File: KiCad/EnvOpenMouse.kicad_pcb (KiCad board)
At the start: 2 copper layers, 34.5 x 42.7 mm, 48 parts, among them J1 SKRKAEE020, J2 SKRKAEE020, J3 Conn_01x03_Male, SW1 MouseSwitch, SW2 MouseSwitch, U1 TCR2EF19, U2 LM3671MF 3.3, U3 PMW3360DM-T2QU, U4 RP2040, Y1 Crystal 3225 12MHz

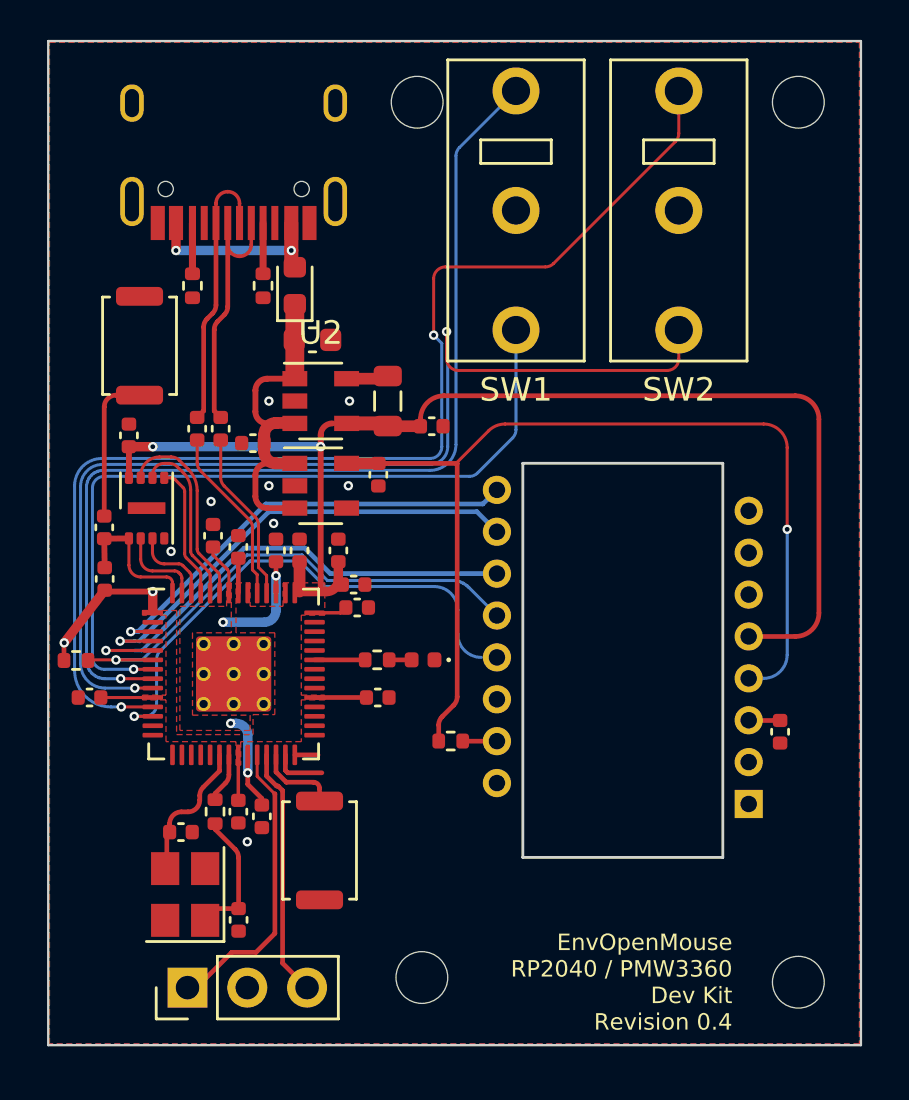
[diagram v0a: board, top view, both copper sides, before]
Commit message: added some GPIO headers
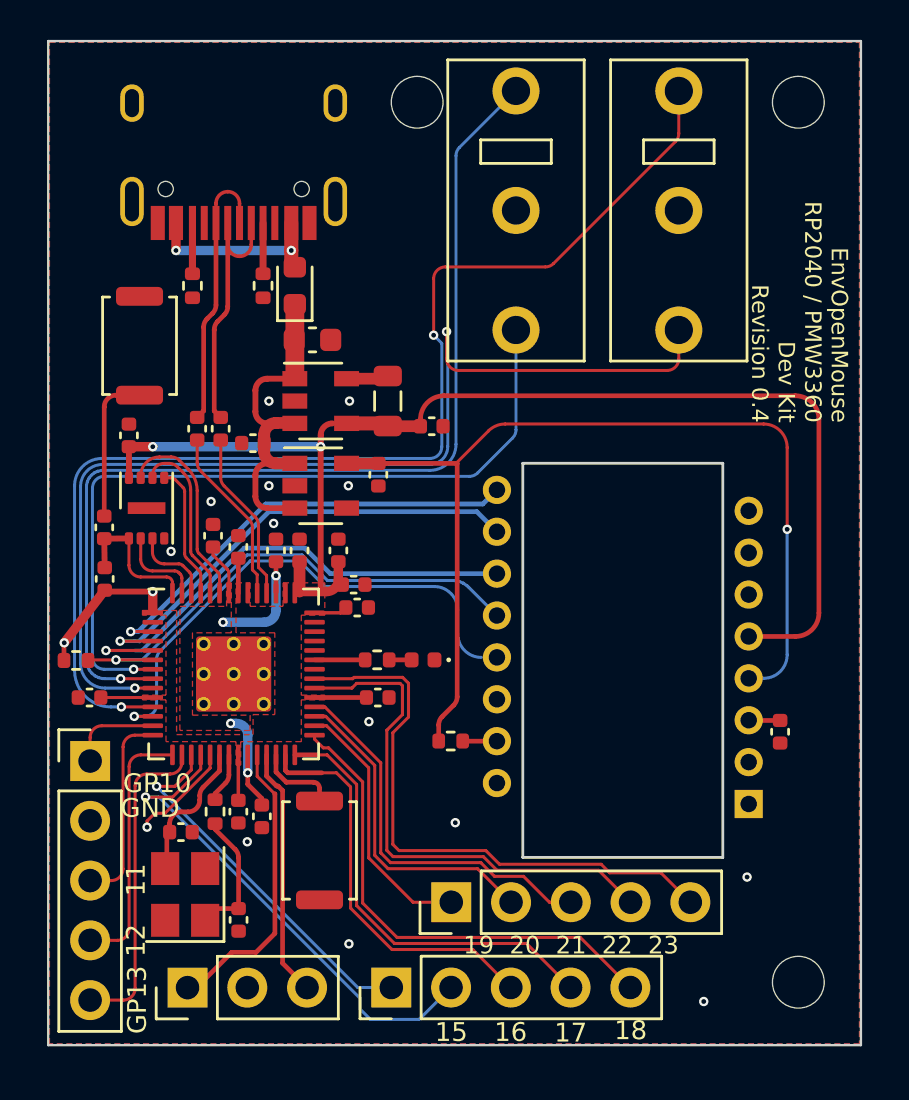
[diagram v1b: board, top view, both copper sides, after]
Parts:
- removed H3: MountingHole, MountingHole:MountingHole_2.2mm_M2
- added GPIOA1: Rotary_Encoder_Switch, Connector_PinHeader_2.54mm:PinHeader_1x05_P2.54mm_Vertical, F.Cu at (52.7, 70.2)
- added GPIOA2: Rotary_Encoder_Switch, Connector_PinHeader_2.54mm:PinHeader_1x05_P2.54mm_Vertical, F.Cu at (55.2, 66.6)
- added SCRL1: Rotary_Encoder_Switch, Connector_PinHeader_2.54mm:PinHeader_1x05_P2.54mm_Vertical, F.Cu at (39.9, 60.6)
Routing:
- net /GPIO23: track 0.00 -> 24.9 mm
- net /GPIO22: track 0.00 -> 22.4 mm
- net /GPIO15: track 0.00 -> 21.2 mm, vias 0 -> 1
- net /GPIO18: track 0.00 -> 21.0 mm
- net /GPIO17: track 0.99 -> 18.8 mm
- net /GPIO21: track 0.00 -> 16.6 mm
- net /GPIO14: track 0.00 -> 15.9 mm, vias 0 -> 1
- net /GPIO16: track 2.25 -> 17.1 mm
- net /GPIO20: track 0.00 -> 13.9 mm
- net /GPIO13: track 0.00 -> 13.6 mm
- net /GPIO19: track 0.00 -> 11.2 mm
- net /GPIO12: track 0.00 -> 10.9 mm
- net /GPIO11: track 0.00 -> 8.37 mm
- net GND: track 0.00 -> 4.43 mm, vias 8 -> 14
- net /GPIO10: track 0.00 -> 3.93 mm
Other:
- board text added: "11"
- board text added: "12"
- board text added: "15"
- board text added: "16"
- board text added: "17"
- board text added: "18"
- board text added: "19 20 21 22 23"
- board text added: "GND"
- board text added: "GP10"
- board text added: "GP13"

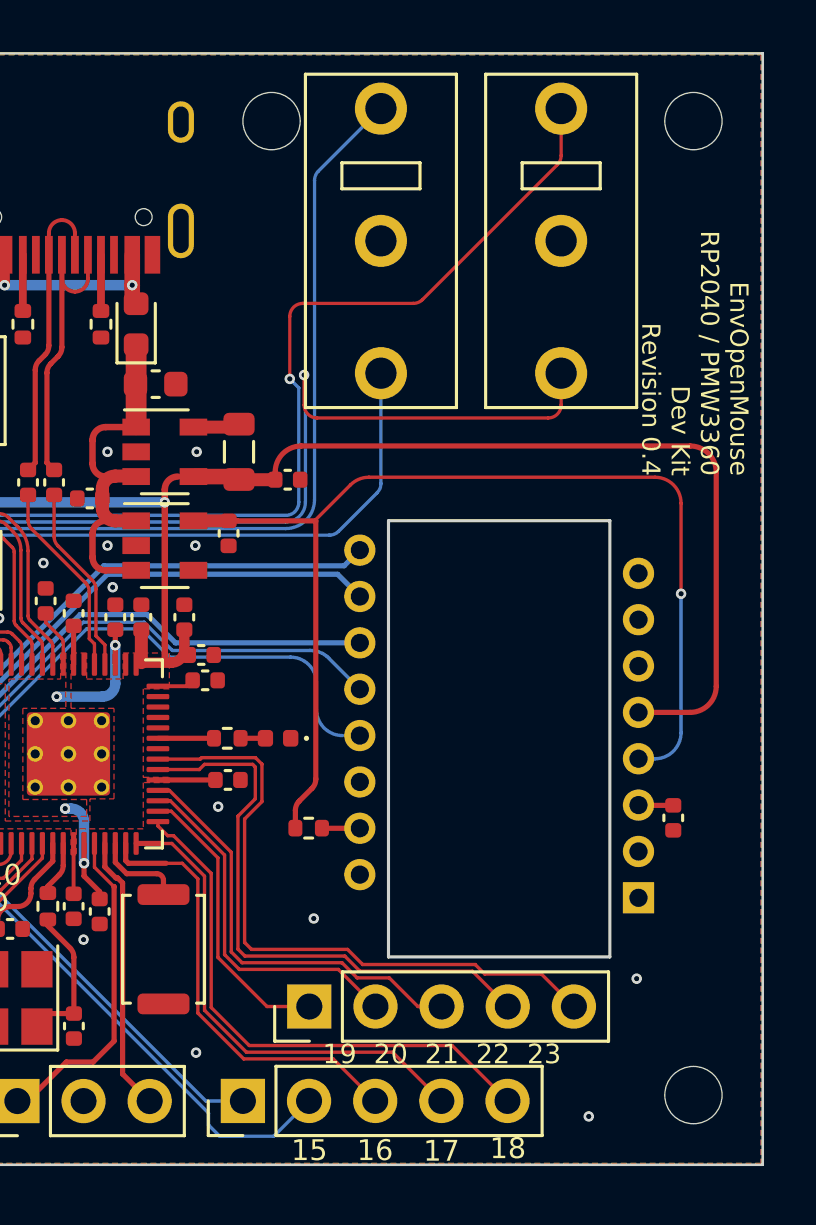
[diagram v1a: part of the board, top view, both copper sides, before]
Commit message: adjusted silkscreen markings and some traces.
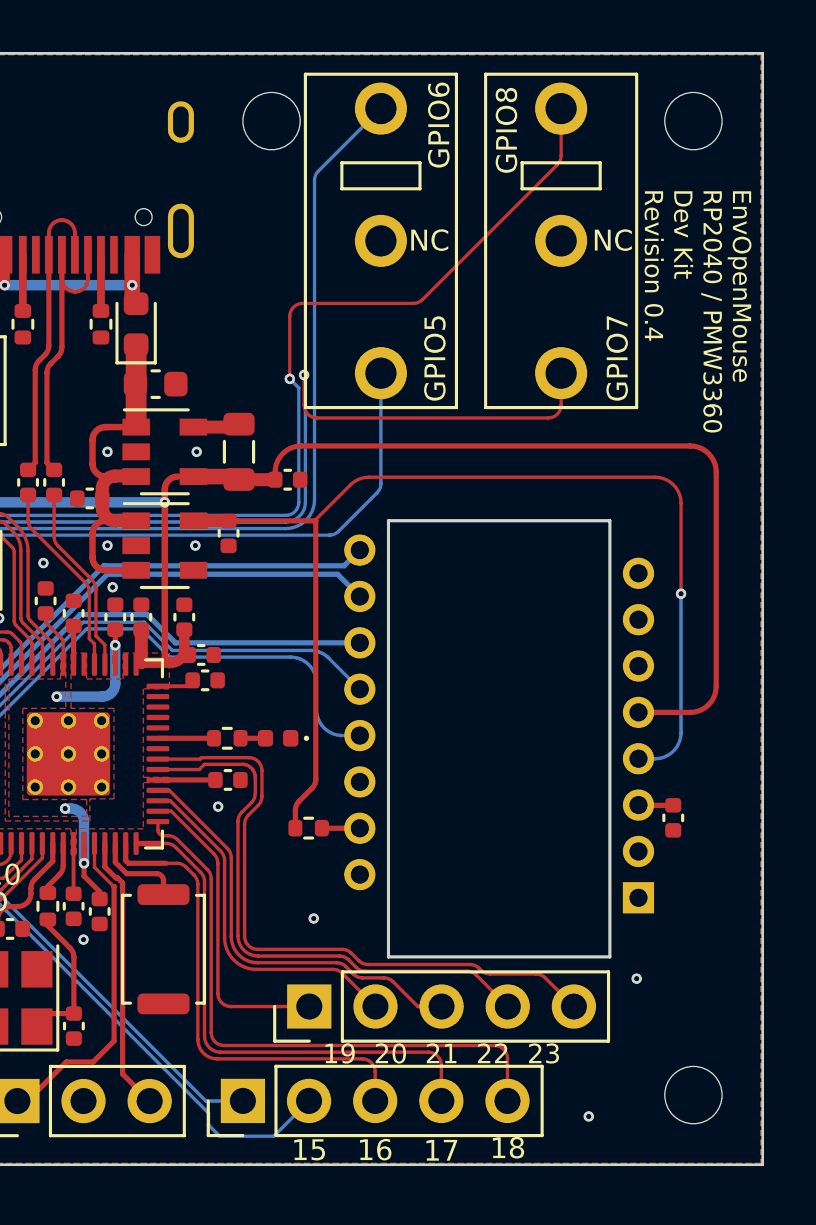
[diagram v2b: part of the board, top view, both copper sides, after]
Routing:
- net /GPIO18: track 21.0 -> 22.7 mm
- net /GPIO17: track 18.8 -> 20.3 mm
- net /GPIO16: track 17.1 -> 18.4 mm
- net /GPIO19: track 11.2 -> 12.0 mm
- net GND: vias 14 -> 13
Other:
- board text added: "GPIO5"
- board text added: "GPIO6"
- board text added: "GPIO7"
- board text added: "GPIO8"
- board text added: "NC"

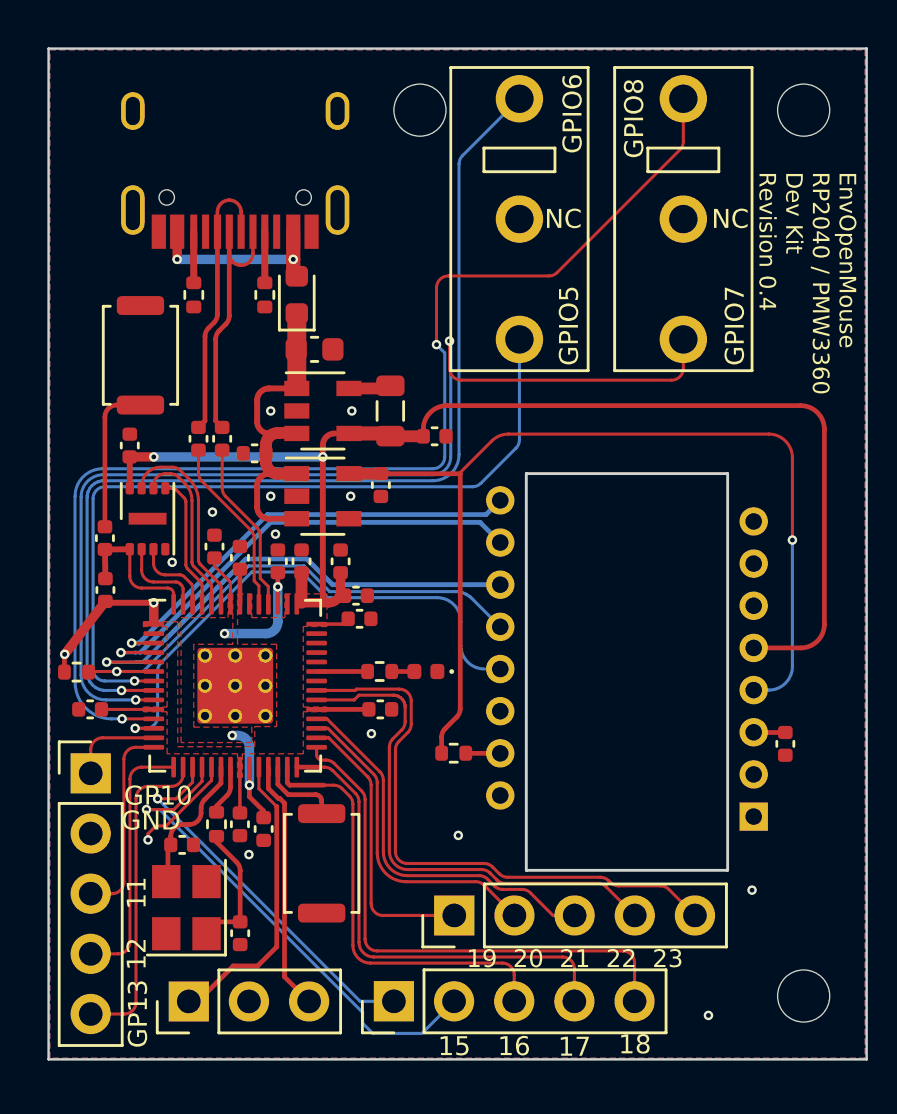
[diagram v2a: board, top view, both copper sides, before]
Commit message: swapped button bits for some GPIO headers
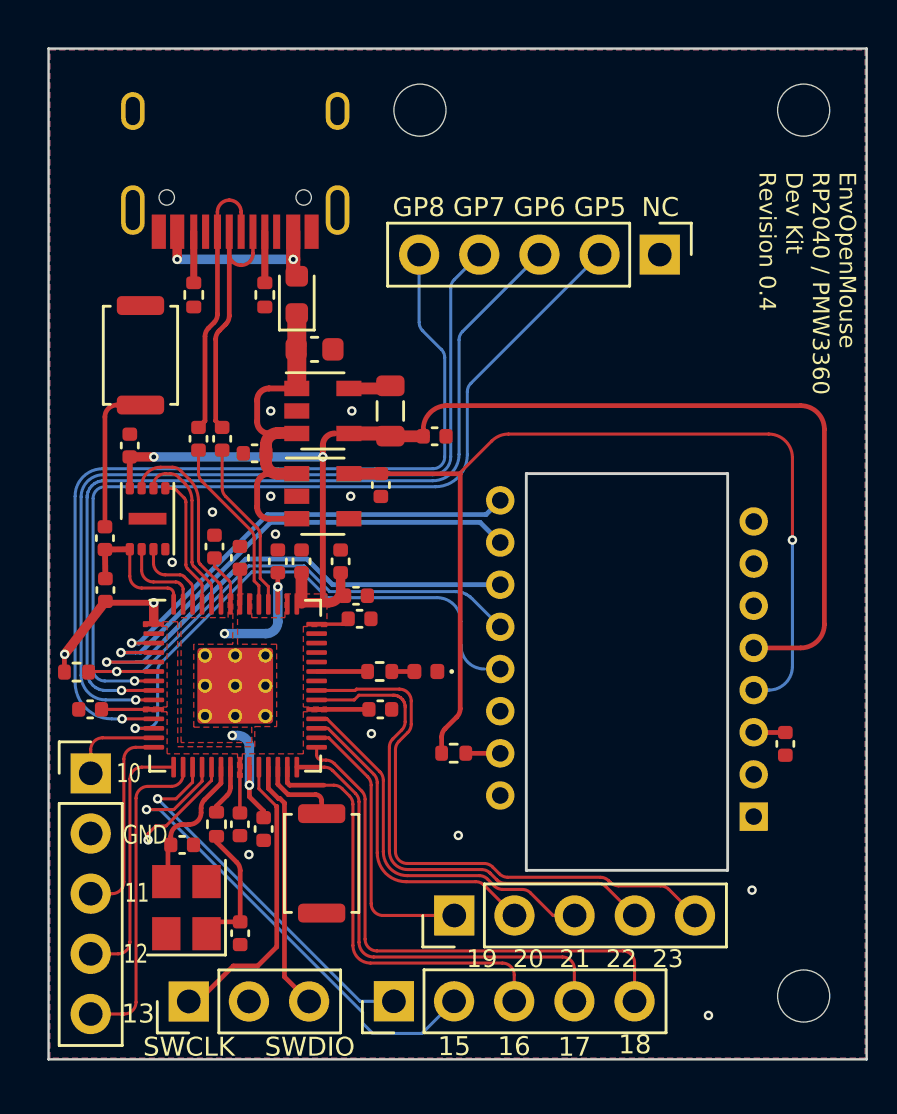
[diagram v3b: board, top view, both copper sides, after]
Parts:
- removed SW1, SW2: MouseSwitch, MouseSwitch:MouseSwitch
- added GPIOA3: GPIOs, Connector_PinHeader_2.54mm:PinHeader_1x05_P2.54mm_Vertical, F.Cu at (63.9, 38.7)
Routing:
- net /GPIO8: track 50.7 -> 37.4 mm, vias 2 -> 1
- net /GPIO7: track 45.4 -> 36.7 mm, vias 2 -> 1
- net /GPIO6: track 43.4 -> 37.1 mm
- net /GPIO5: track 33.5 -> 37.6 mm
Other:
- board text added: "10"
- board text added: "13"
- board text added: "GP5"
- board text added: "GP6"
- board text added: "GP7"
- board text added: "GP8"
- board text added: "SWCLK"
- board text added: "SWDIO"
- board text removed: "GP10"
- board text removed: "GP13"
- board text removed: "GPIO5"
- board text removed: "GPIO6"
- board text removed: "GPIO7"
- board text removed: "GPIO8"

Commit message: decided to overhaul this project a bit
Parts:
- removed C10, C11, C12, C13, C14, C17, C6, C7, C8, C9: 100nf 0402, Capacitor_SMD:C_0402_1005Metric
- removed C15, C16: 1uf 0402, Capacitor_SMD:C_0402_1005Metric
- removed C18, C19: 22pf 0402, Capacitor_SMD:C_0402_1005Metric
- removed C4: 10uf 0402, Capacitor_SMD:C_0402_1005Metric
- removed C5: 4.7uf 0402, Capacitor_SMD:C_0402_1005Metric
- removed D1: 1n4002 0603, Diode_SMD:D_0603_1608Metric
- removed D2: LED 0402 YELLOW, LED_SMD:LED_0402_1005Metric
- removed FLASH1: W25Q16FWUXIE, Package_SON:SON-8-1EP_3x2mm_P0.5mm_EP1.4x1.6mm
- removed GPIOA1, GPIOA2, SCRL1: Rotary_Encoder_Switch, Connector_PinHeader_2.54mm:PinHeader_1x05_P2.54mm_Vertical
- removed GPIOA3: GPIOs, Connector_PinHeader_2.54mm:PinHeader_1x05_P2.54mm_Vertical
- removed L1: INDUCTOR 2.2uH 0805, Inductor_SMD:L_0805_2012Metric
- removed R10: 1K 0402, Resistor_SMD:R_0402_1005Metric
- removed R3: 10K 0402, Resistor_SMD:R_0402_1005Metric
- removed R4: 5.1K, Resistor_SMD:R_0402_1005Metric
- removed R5: 10K 0402, Capacitor_SMD:C_0402_1005Metric
- removed R6, R7: 27Ohms 0402 Resistor, Capacitor_SMD:C_0402_1005Metric
- removed R8: 1k 0402 Resistor, Capacitor_SMD:C_0402_1005Metric
- removed R9: 470 ohm resistor, Resistor_SMD:R_0402_1005Metric
- removed U3: PMW3360DM-T2QU, local:DIP-16_W10.16mm
- removed U4: RP2040, env:RP2040-QFN-56
- removed Y1: Crystal 3225 12MHz, Crystal:Crystal_SMD_3225-4Pin_3.2x2.5mm
- removed e1: TYPE-C-31-M-12, Type-C:HRO-TYPE-C-31-M-12-Assembly
- added H10: MountingHole_Pad, MountingHole:MountingHole_2.2mm_M2, F.Cu at (57.5, 15.1)
- added H3: MountingHole_Pad, MountingHole:MountingHole_2.2mm_M2, F.Cu at (50.0, 15.0)
- added H5: MountingHole_Pad, MountingHole:MountingHole_2.2mm_M2, F.Cu at (33.5, 40.2)
- added H6: MountingHole_Pad, MountingHole:MountingHole_2.2mm_M2, F.Cu at (16.4, 14.9)
- added H7: MountingHole_Pad, MountingHole:MountingHole_2.2mm_M2, F.Cu at (33.5, 14.9)
- added H8: MountingHole_Pad, MountingHole:MountingHole_2.2mm_M2, F.Cu at (16.4, 40.2)
- added H9: MountingHole_Pad, MountingHole:MountingHole_2.2mm_M2, F.Cu at (60.1, 40.0)
- added J4: Conn_01x03, Connector_PinHeader_2.54mm:PinHeader_1x03_P2.54mm_Vertical, F.Cu at (62.6, 34.9)
- added SW1: SW_Push_SPDT, MouseSwitch:MouseSwitch, F.Cu at (40.7, 23.9)
- added SW2: SW_Push_SPDT, MouseSwitch:MouseSwitch, F.Cu at (50.0, 24.0)
- added VR1: EC10E1220501, EC10E1220501:TRIM_EC10E1220501, F.Cu at (60.8, 21.8)
- C1: value 10uf 0603 6.3V -> 0.1uf 0402; footprint Capacitor_SMD:C_0603_1608Metric -> Capacitor_SMD:C_0201_0603Metric
- C2: value 0.1uf 0402 -> 1uf 0402; footprint Capacitor_SMD:C_0402_1005Metric -> Capacitor_SMD:C_0201_0603Metric
- C3: value 1uf 0402 -> 4.7uf 0402; footprint Capacitor_SMD:C_0402_1005Metric -> Capacitor_SMD:C_0201_0603Metric
- H1, H2, H4: value MountingHole -> MountingHole_Pad
- J1: value SKRKAEE020 -> Conn_01x08; footprint Button_Switch_SMD:SW_Push_SPST_NO_Alps_SKRK -> Connector_PinHeader_1.00mm:PinHeader_1x08_P1.00mm_Vertical
- J2: value SKRKAEE020 -> Conn_01x03; footprint Button_Switch_SMD:SW_Push_SPST_NO_Alps_SKRK -> Connector_PinSocket_2.54mm:PinSocket_1x03_P2.54mm_Vertical
- J3: value Conn_01x03_Male -> Conn_01x03; footprint Connector_PinHeader_2.54mm:PinHeader_1x03_P2.54mm_Vertical -> Connector_PinSocket_2.54mm:PinSocket_1x03_P2.54mm_Vertical
- R2: value 5.1K -> 10K 0402
- U2: value LM3671MF 3.3 -> PMW3360DM-T2QU; footprint Package_TO_SOT_SMD:SOT-23-5 -> local:DIP-16_W10.16mm
- moved U1 43.2 mm to (17.6, 19.9)
- moved R1 41.7 mm to (33.9, 24.0), turned to 180 degrees
- moved C1 40.9 mm to (14.8, 20.9)
- moved C3 39.9 mm to (20.2, 24.6)
- moved C2 39.0 mm to (19.9, 18.9), turned to -90 degrees
- moved H4 38.7 mm to (50.0, 36.8)
- moved J3 38.0 mm to (47.5, 32.4)
- moved U2 37.2 mm to (22.6, 19.8)
- moved H1 34.2 mm to (40.7, 14.9)
- moved J2 34.0 mm to (38.1, 32.4), turned to 90 degrees
- moved J1 27.4 mm to (17.6, 30.5), turned to 180 degrees
- moved R2 17.4 mm to (33.9, 29.3), turned to 180 degrees
- moved H2 13.8 mm to (40.7, 36.8)
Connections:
- C1 pad 1: +5V -> GND
- C1 pad 2: GND -> +5V
- C2 pad 2: +5V -> +1V8
- C3 pad 1: GND -> Net-(C3-Pad1)
- C3 pad 2: +1V8 -> GND
- J1 pad 1: /~{USB_BOOT} -> NCS/GPIO9
- J1 pad 2: GND -> MISO/GPIO4
- J2 pad 1: /RUN -> Net-(J2-Pad1)
- J2 pad 2: GND -> Net-(J2-Pad2)
- J3 pad 1: /SWCLK -> Net-(J3-Pad1)
- J3 pad 2: GND -> Net-(J3-Pad2)
- J3 pad 3: /SWD -> Net-(J3-Pad3)
- R2 pad 1: GND -> +3V3
- R2 pad 2: Net-(R2-Pad2) -> MISO/GPIO4
- U2 pad 1: +5V -> unconnected-(U2-Pad1)
- U2 pad 2: GND -> unconnected-(U2-Pad2)
- U2 pad 3: +5V -> Net-(C3-Pad1)
- U2 pad 4: +3V3 -> +1V8
- U2 pad 5: Net-(L1-Pad1) -> +3V3
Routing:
- net /GPIO5: track 37.6 -> 0.00 mm, vias 1 -> 0
- net /GPIO8: track 37.4 -> 0.00 mm, vias 1 -> 0
- net /GPIO6: track 37.1 -> 0.00 mm, vias 1 -> 0
- net /GPIO7: track 36.7 -> 0.00 mm, vias 1 -> 0
- net NCS/GPIO9: track 0.00 -> 34.4 mm
- net MISO/GPIO4: track 0.00 -> 31.6 mm
- net +3V3: track 69.6 -> 38.0 mm, vias 4 -> 1
- net MOSI/GPIO3: track 0.00 -> 28.9 mm
- net SCLK/GPIO2: track 0.00 -> 26.7 mm
- net /GPIO23: track 24.6 -> 0.00 mm
- net MOTION/GPIO1: track 0.00 -> 23.8 mm
- net /GPIO18: track 22.7 -> 0.00 mm
- net NCS: track 22.1 -> 0.00 mm, vias 1 -> 0
- net /GPIO22: track 21.9 -> 0.00 mm
- net MISO: track 21.8 -> 0.00 mm, vias 1 -> 0
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- removed copper zone on F.Cu, net +1V1
- removed copper zone on F.Cu, net +3V3
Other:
- board size 34.5 x 42.7 mm -> 52.3 x 30.4 mm
- board text added: "A/B/C"
- board text added: "GND 5V 3.3V MOT/GP1 SCLK/GP2 MOSI/GP3 MISO/GP4 NCS/GP9"
- board text added: "Github.com/envious-data"
- board text removed: "10"
- board text removed: "11"
- board text removed: "12"
- board text removed: "13"
- board text removed: "15"
- board text removed: "16"
- board text removed: "17"
- board text removed: "18"
- board text removed: "19 20 21 22 23"
- board text removed: "EnvOpenMouse RP2040 / PMW3360 Dev Kit Revision 0.4"
- board text removed: "GND"
- board text removed: "GP5"
- board text removed: "GP6"
- board text removed: "GP7"
- board text removed: "GP8"
- board text removed: "NC"
- board text removed: "SWCLK"
- board text removed: "SWDIO"

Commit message: small fix
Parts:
- J2, J3: footprint Connector_PinSocket_2.54mm:PinSocket_1x03_P2.54mm_Vertical -> Connector_PinHeader_2.54mm:PinHeader_1x03_P2.54mm_Vertical
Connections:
- VR1 pad : GND -> (no net)
